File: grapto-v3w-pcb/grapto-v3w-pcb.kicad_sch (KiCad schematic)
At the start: 35 parts

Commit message: Before removing pmux.
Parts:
- removed TH?: Thermistor_PTC, symbol Device:Thermistor_PTC
- added F?: Polyfuse, symbol Device:Polyfuse
- added JP? (x3): SolderJumper_2_Bridged, symbol Jumper:SolderJumper_2_Bridged
- added TP? (x6): TestPoint, symbol Connector:TestPoint
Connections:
- net P+: now also C?.1, U?.6 (BATT)
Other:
- note added: "Power dissipation for shunt? Low or high-side shunt?"
- note added: "TODO: Double check nrf52840 max current draw"

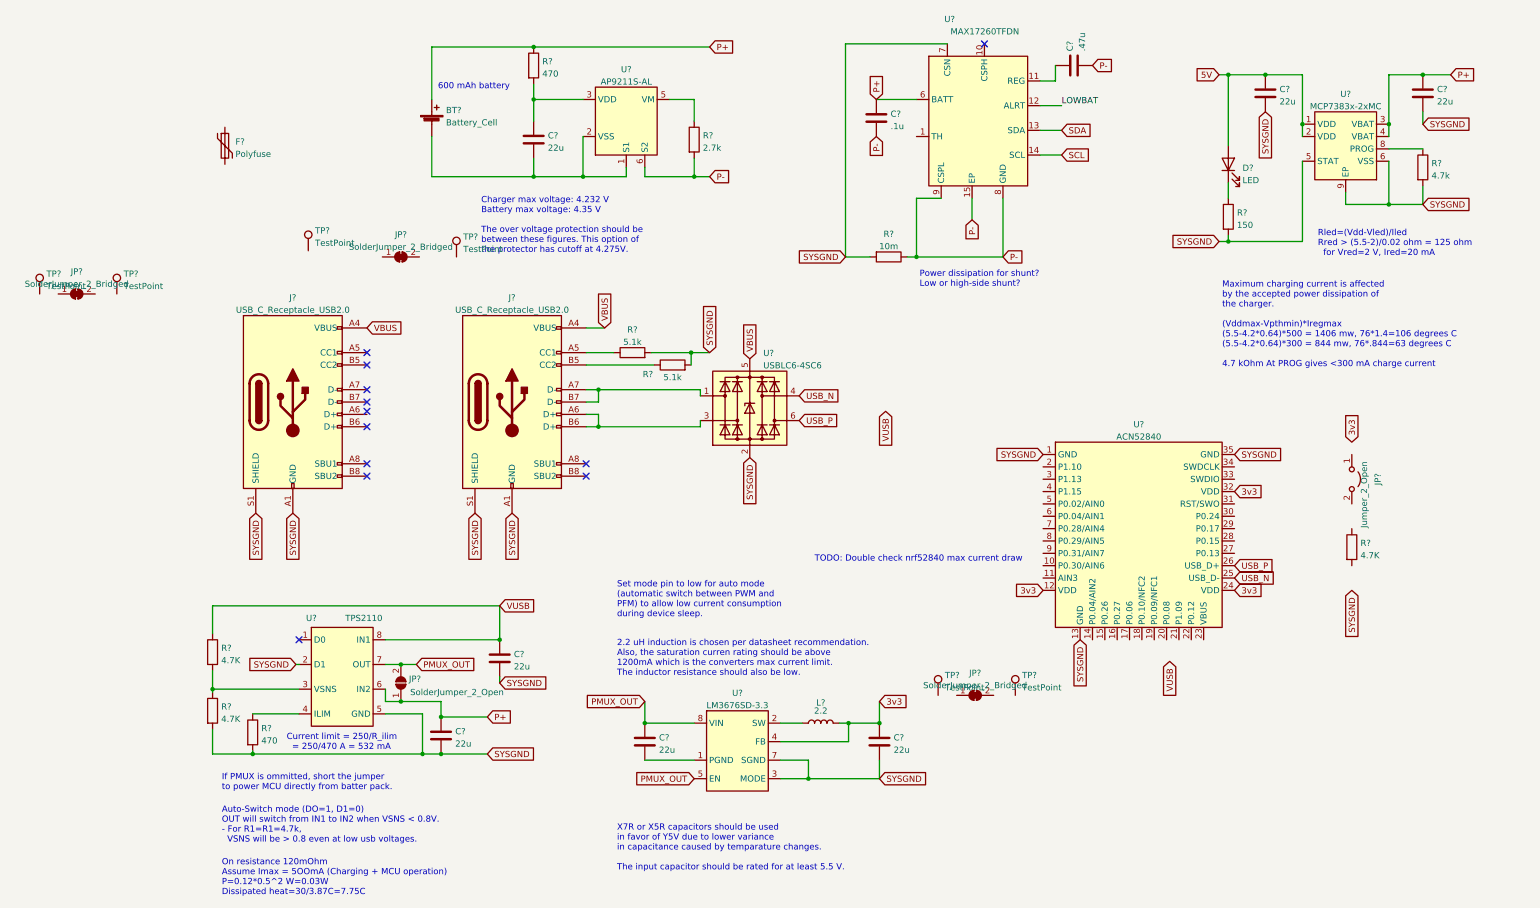
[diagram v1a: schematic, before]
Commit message: First draft of controller pcb
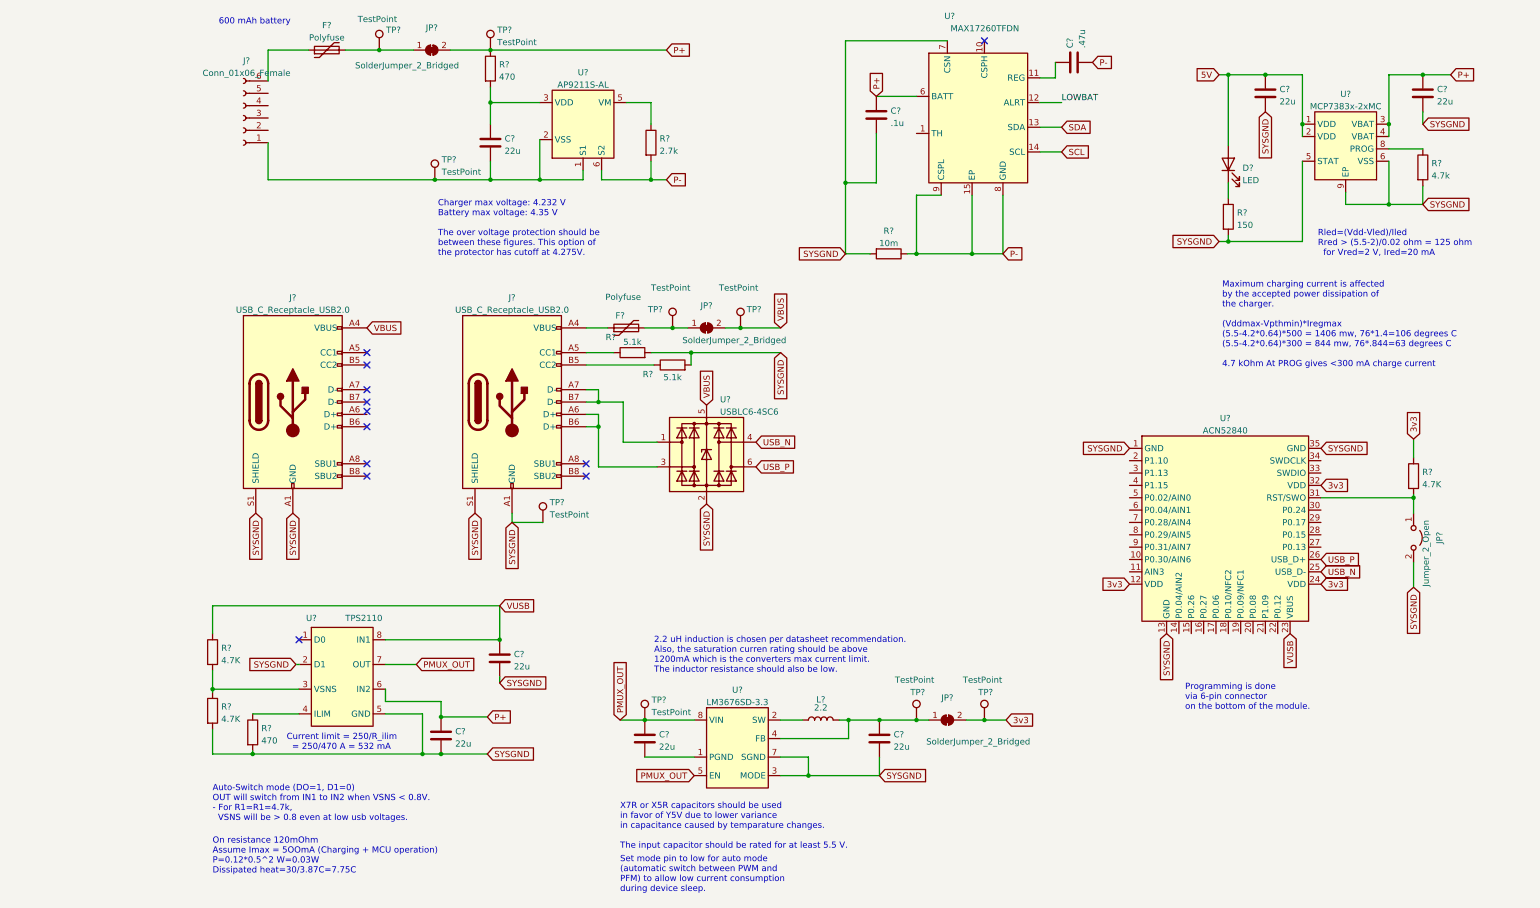
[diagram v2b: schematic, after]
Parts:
- removed BT?: Battery_Cell, symbol Device:Battery_Cell
- removed JP?: SolderJumper_2_Open, symbol Jumper:SolderJumper_2_Open
- removed JP?: SolderJumper_2_Bridged, symbol Jumper:SolderJumper_2_Bridged
- removed TP? (x2): TestPoint, symbol Connector:TestPoint
- added F?: Polyfuse, symbol Device:Polyfuse
- added J?: Conn_01x06_Female, symbol Connector:Conn_01x06_Female
- added JP?: SolderJumper_2_Bridged, symbol Jumper:SolderJumper_2_Bridged
- added TP? (x5): TestPoint, symbol Connector:TestPoint
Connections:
- net 3v3: now also R?.1, JP?.2 (B), TP?.1; no longer C?.1, L?.2, U?.4 (FB)
- net P+: now also JP?.2 (B), TP?.1
- net P-: no longer C?.2
- net PMUX_OUT: now also TP?.1
- net SYSGND: now also C?.2, JP?.2 (B), TP?.1
- net VBUS: now also JP?.2 (B), TP?.1; no longer J?.A4 (VBUS), J?.A9 (VBUS), J?.B4 (VBUS), J?.B9 (VBUS)
- net VUSB: now also U?.23 (VBUS)
- net at JP?.1 (A): now also F?.2, TP?.1
- net at F?.1: now also J?.6 (Pin_6)
- net at R?.2: now also JP?.1 (A), U?.31 (RST/SWO)
- net at C?.2, U?.1 (S1), U?.2 (VSS): now also J?.1 (Pin_1), TP?.1
- net at TP?.1: now also JP?.1 (A), F?.2
- new net: F?.1, J?.A4 (VBUS), J?.A9 (VBUS), J?.B4 (VBUS), J?.B9 (VBUS)
- new net: C?.1, JP?.1 (A), L?.2, TP?.1, U?.4 (FB)
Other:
- note added: "Programming is done via 6-pin connector on the bottom of the module."
- note removed: "If PMUX is ommitted, short the jumper to power MCU directly from batter pack."
- note removed: "Power dissipation for shunt? Low or high-side shunt?"
- note removed: "TODO: Double check nrf52840 max current draw"
- moved on the sheet: C?, F?, JP?, L?, R?, TP?, U?

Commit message: Began experimenting with modules
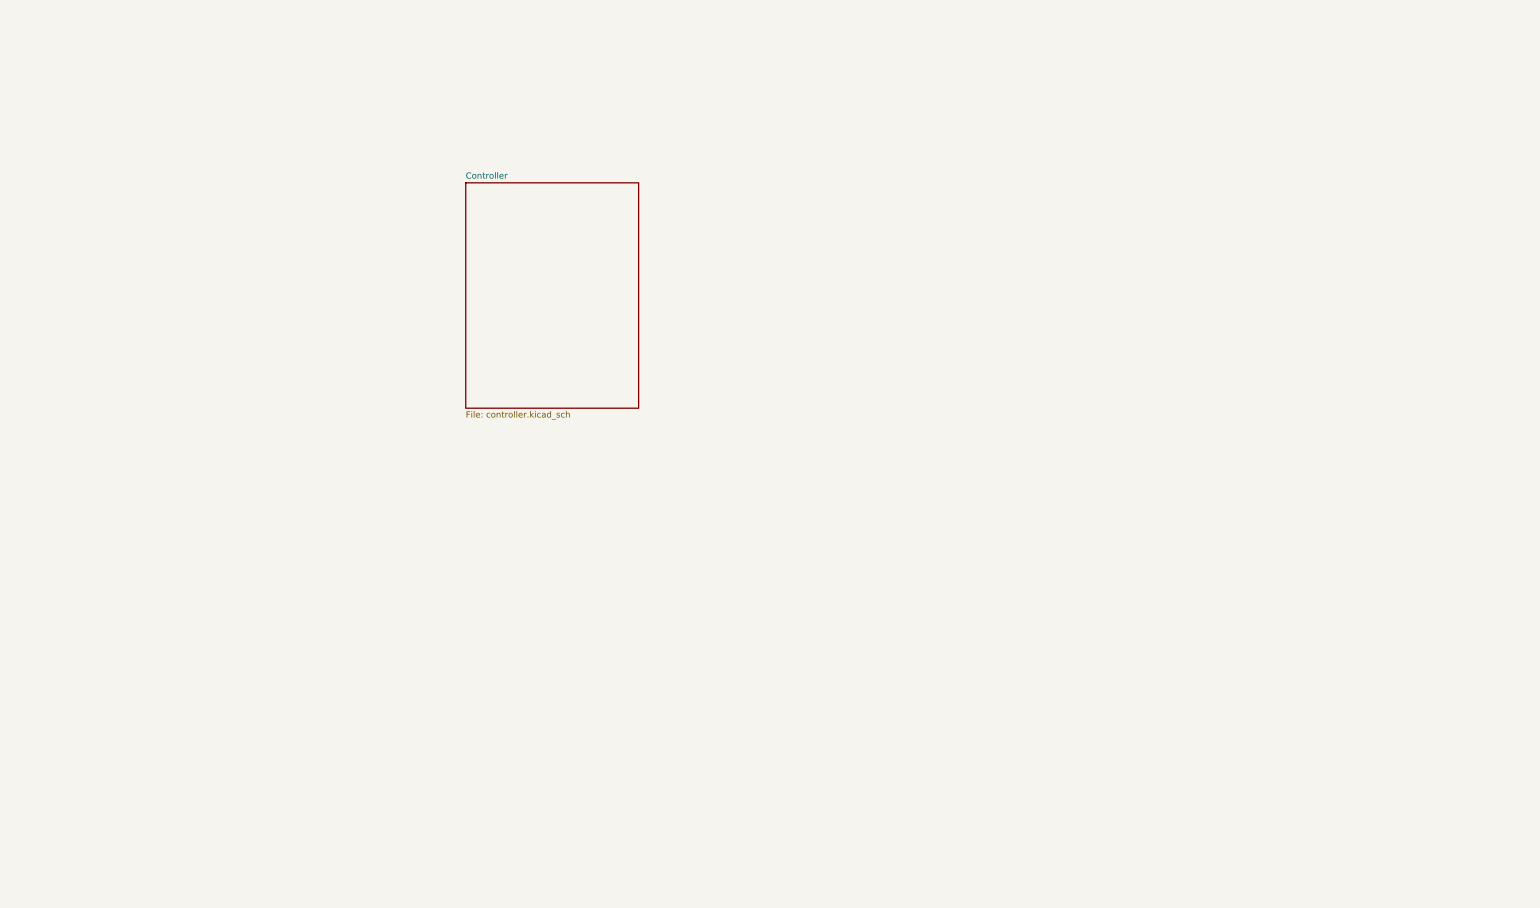
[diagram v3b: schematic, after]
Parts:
- removed C? (x7): 22u, symbol Device:C
- removed C?: .47u, symbol Device:C
- removed C?: .1u, symbol Device:C
- removed D?: LED, symbol Device:LED
- removed F? (x2): Polyfuse, symbol Device:Polyfuse
- removed J? (x2): USB_C_Receptacle_USB2.0, symbol Connector:USB_C_Receptacle_USB2.0
- removed J?: Conn_01x06_Female, symbol Connector:Conn_01x06_Female
- removed JP? (x3): SolderJumper_2_Bridged, symbol Jumper:SolderJumper_2_Bridged
- removed JP?: Jumper_2_Open, symbol Jumper:Jumper_2_Open
- removed L?: 2.2, symbol Device:L
- removed R?: 150, symbol Device:R
- removed R? (x2): 470, symbol Device:R
- removed R? (x3): 4.7K, symbol Device:R
- removed R?: 10m, symbol Device:R
- removed R? (x2): 5.1k, symbol Device:R
- removed R?: 2.7k, symbol Device:R
- removed R?: 4.7k, symbol Device:R
- removed TP? (x9): TestPoint, symbol Connector:TestPoint
- removed U?: MCP7383x-2xMC, symbol grapto-v3w:MCP7383x-2xMC
- removed U?: LM3676SD-3.3, symbol grapto-v3w:LM3676SD-3.3
- removed U?: MAX17260TFDN, symbol grapto-v3w:MAX17260TFDN
- removed U?: USBLC6-4SC6, Package_TO_SOT_SMD:SOT-23-6, symbol Power_Protection:USBLC6-4SC6
- removed U?: ACN52840, symbol grapto-v3w:ACN52840
- removed U?: TPS2110, symbol grapto-v3w:TPS2110
- removed U?: AP9211S-AL, symbol grapto-v3w:AP9211S-AL
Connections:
- no-connect marks 12 -> 0
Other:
- added sheet Controller (controller.kicad_sch)
- note removed: "2.2 uH induction is chosen per datasheet recommendation. Also, the saturation curren rating should be above 1200mA which is the converters max current limit. The inductor resistance should also be low."
- note removed: "600 mAh battery"
- note removed: "Auto-Switch mode (DO=1, D1=0) OUT will switch from IN1 to IN2 when VSNS < 0.8V. - For R1=R1=4.7k, VSNS will be > 0.8 even at low usb voltages."
- note removed: "Charger max voltage: 4.232 V Battery max voltage: 4.35 V The over voltage protection should be between these figures. This option of the protector has cutoff at 4.275V."
- note removed: "Current limit = 250/R_ilim = 250/470 A = 532 mA"
- note removed: "Maximum charging current is affected by the accepted power dissipation of the charger. (Vddmax-Vpthmin)*Iregmax (5.5-4.2*0.64)*500 = 1406 mw, 76*1.4=106 degrees C (5.5-4.2*0.64)*300 = 844 mw, 76*.844=63 degrees C 4.7 kOhm At PROG gives <300 mA charge current"
- note removed: "On resistance 120mOhm Assume Imax = 5OOmA (Charging + MCU operation) P=0.12*0.5^2 W=0.03W Dissipated heat=30/3.87C=7.75C"
- note removed: "Programming is done via 6-pin connector on the bottom of the module."
- note removed: "Rled=(Vdd-Vled)/Iled Rred > (5.5-2)/0.02 ohm = 125 ohm for Vred=2 V, Ired=20 mA"
- note removed: "Set mode pin to low for auto mode (automatic switch between PWM and PFM) to allow low current consumption during device sleep."
- note removed: "X7R or X5R capacitors should be used in favor of Y5V due to lower variance in capacitance caused by temparature changes. The input capacitor should be rated for at least 5.5 V."

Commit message: Think i got modules working.
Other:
- added sheet Controller1 (controller.kicad_sch)

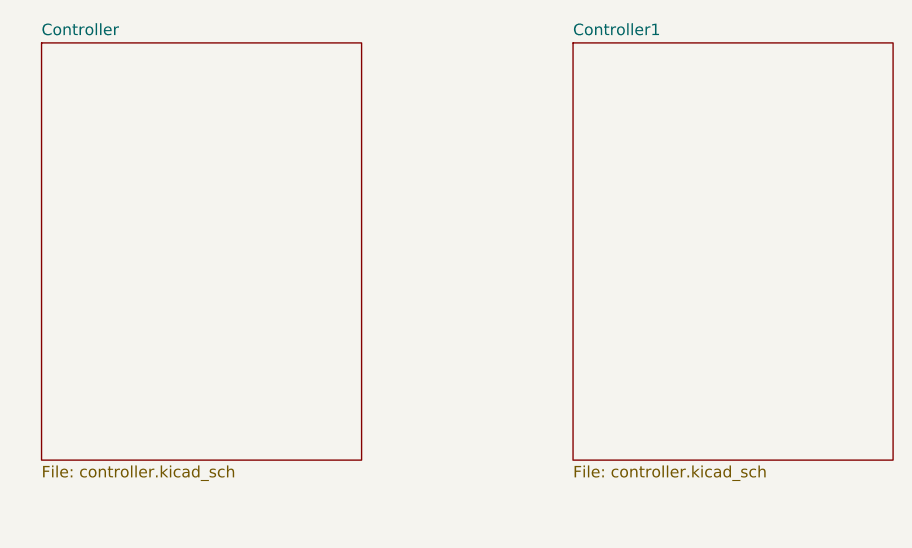
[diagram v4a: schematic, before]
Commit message: Added keymatrix.
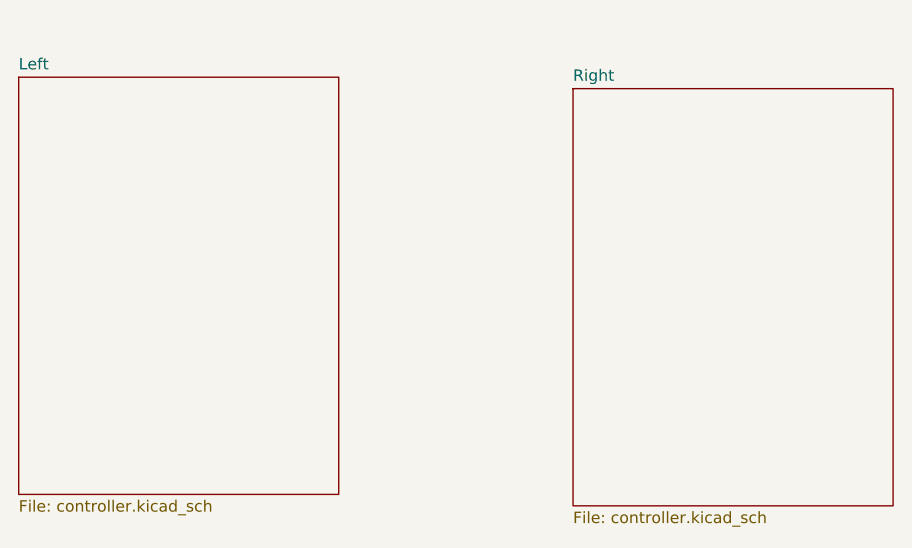
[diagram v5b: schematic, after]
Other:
- sheet Controller renamed Right
- sheet Controller1 renamed Left
